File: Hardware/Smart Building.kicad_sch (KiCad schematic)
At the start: 11 parts, among them J2 DHT11, J3 Screw_Terminal_01x03, J4 Screw_Terminal_01x03, J5 Conn_01x06_Pin, J6 ZMPT101b, J7 ACS712, K1 Relay_SPDT, K2 Relay_SPDT, U1 ESP32-DEVKIT-V1

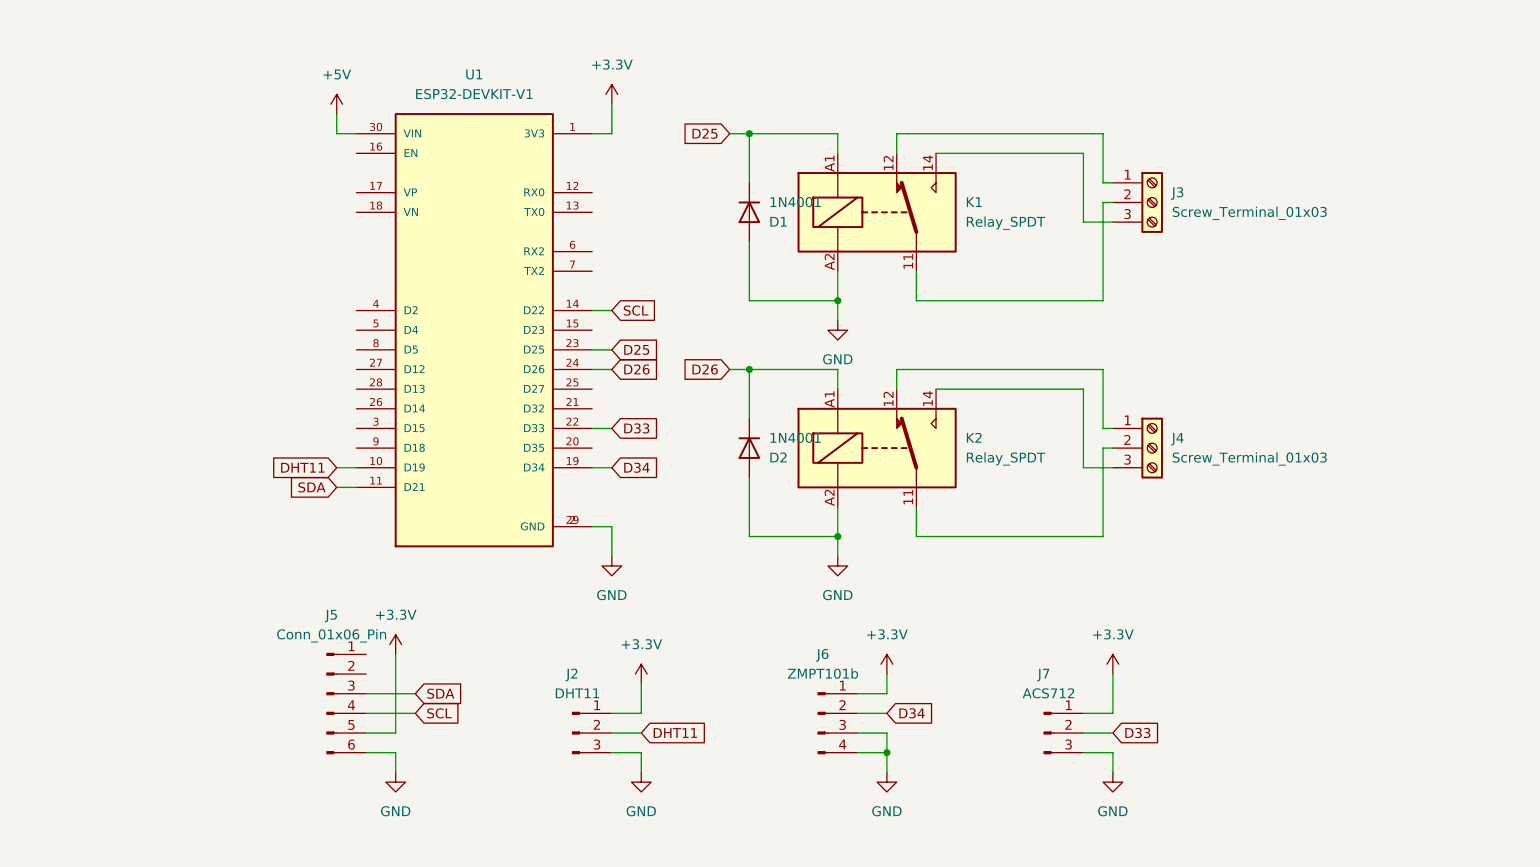
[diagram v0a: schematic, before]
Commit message: memperbarui rangkaian chematic dan board dengan menambahkan sensor tegangan baterai
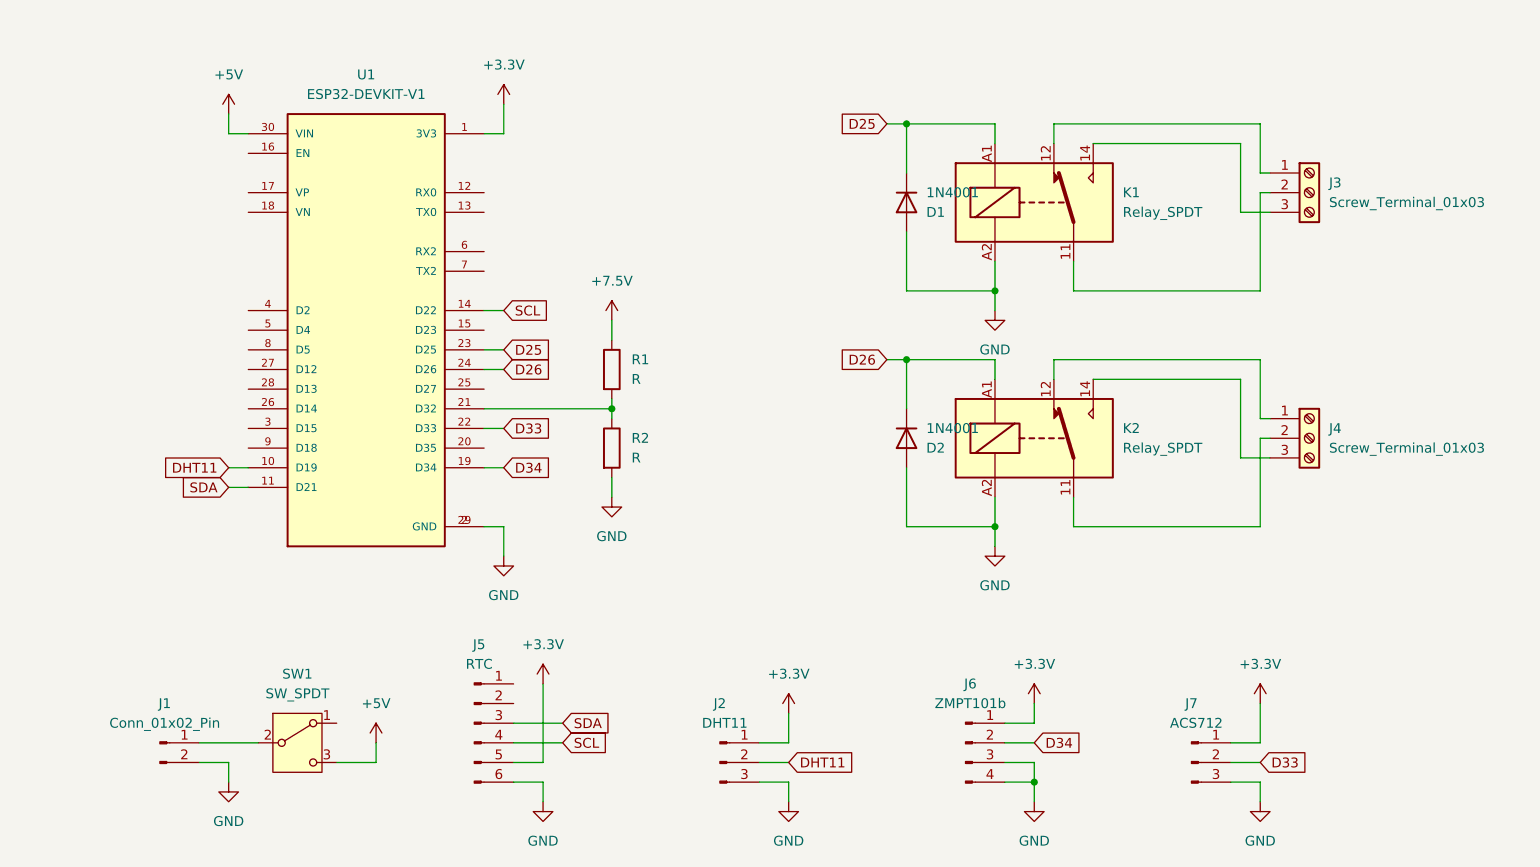
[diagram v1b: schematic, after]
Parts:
- added J1: Conn_01x02_Pin, Connector_JST:JST_EH_B2B-EH-A_1x02_P2.50mm_Vertical, symbol Connector:Conn_01x02_Pin
- added R1, R2: R, Resistor_THT:R_Axial_DIN0207_L6.3mm_D2.5mm_P10.16mm_Horizontal, symbol Device:R
- added SW1: SW_SPDT, Button_Switch_THT:SW_Slide-03_Wuerth-WS-SLTV_10x2.5x6.4_P2.54mm, symbol Switch:SW_SPDT
- J5: value Conn_01x06_Pin -> RTC
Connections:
- net +5V: now also SW1.3 (C)
- net GND: now also J1.2 (Pin_2), R2.2
- net at U1.21 (D32): now also R1.2, R2.1
- new net: J1.1 (Pin_1), SW1.2 (B)
- new net +7.5V: R1.1
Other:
- company: (none) -> GriyaTech
- title: (none) -> SMART BUILDING
- moved on the sheet: D1, D2, J2, J3, J4, J5, J6, J7, K1, K2, U1

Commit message: memperbarui rangkaian chematic dan board dengan menambahkan opto coupler pc817 untuk mengaktifkan relay yang membutuhkan supply 5v
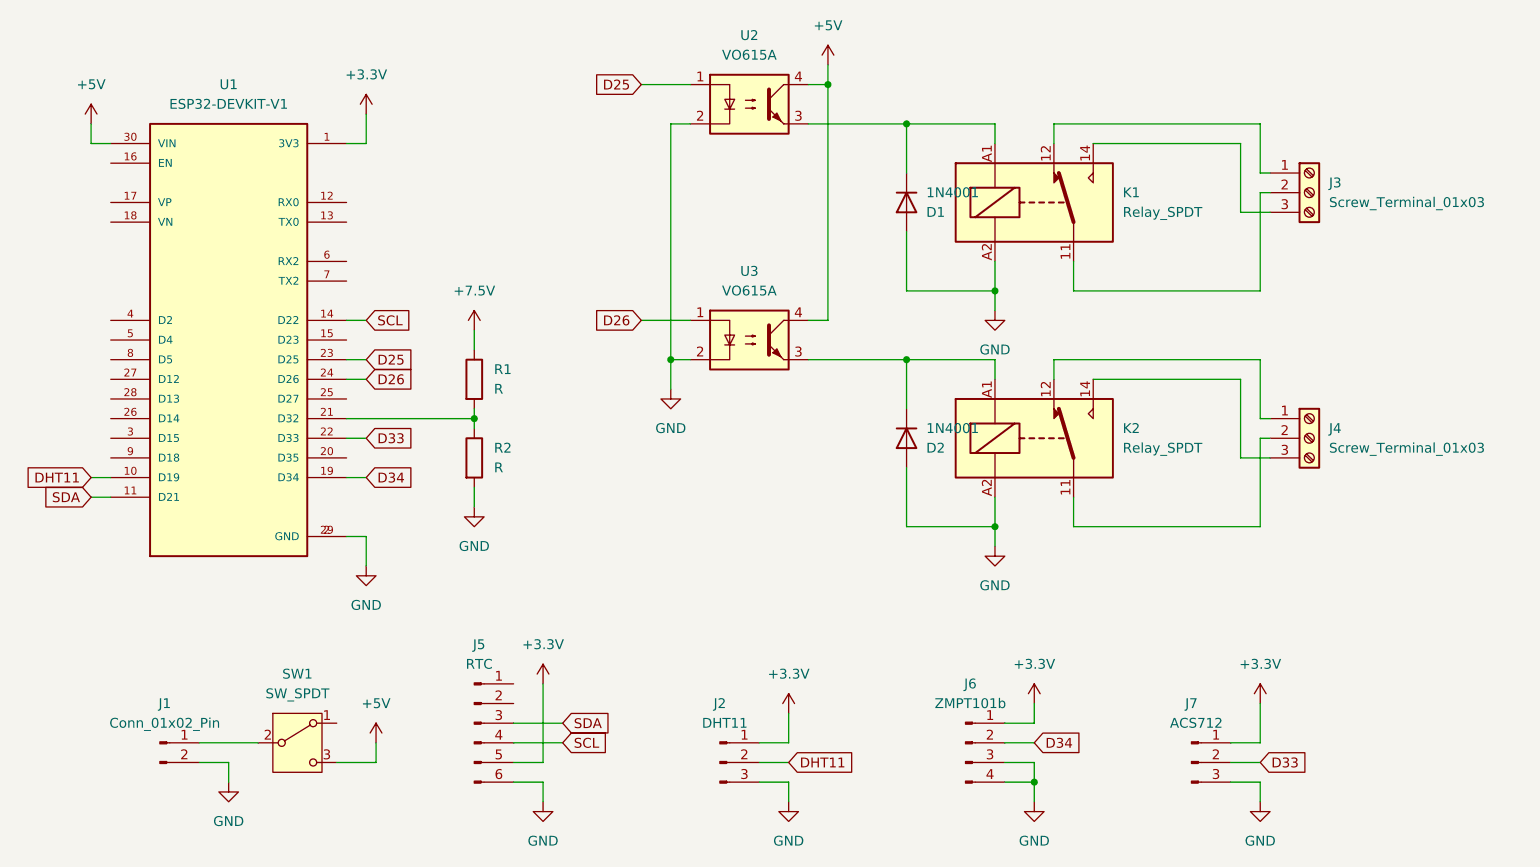
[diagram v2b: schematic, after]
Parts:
- added U2, U3: VO615A, OptoDevice:Everlight_ITR8307F43, symbol Isolator:VO615A
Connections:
- net +5V: now also U2.4, U3.4
- net D25: now also U2.1; no longer D1.1 (K), K1.A1
- net D26: now also U3.1; no longer D2.1 (K), K2.A1
- net GND: now also U2.2, U3.2
- new net: D1.1 (K), K1.A1, U2.3
- new net: D2.1 (K), K2.A1, U3.3
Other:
- moved on the sheet: R1, R2, U1
